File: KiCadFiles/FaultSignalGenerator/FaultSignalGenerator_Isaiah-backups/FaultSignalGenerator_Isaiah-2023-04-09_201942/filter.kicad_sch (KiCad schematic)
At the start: 65 parts

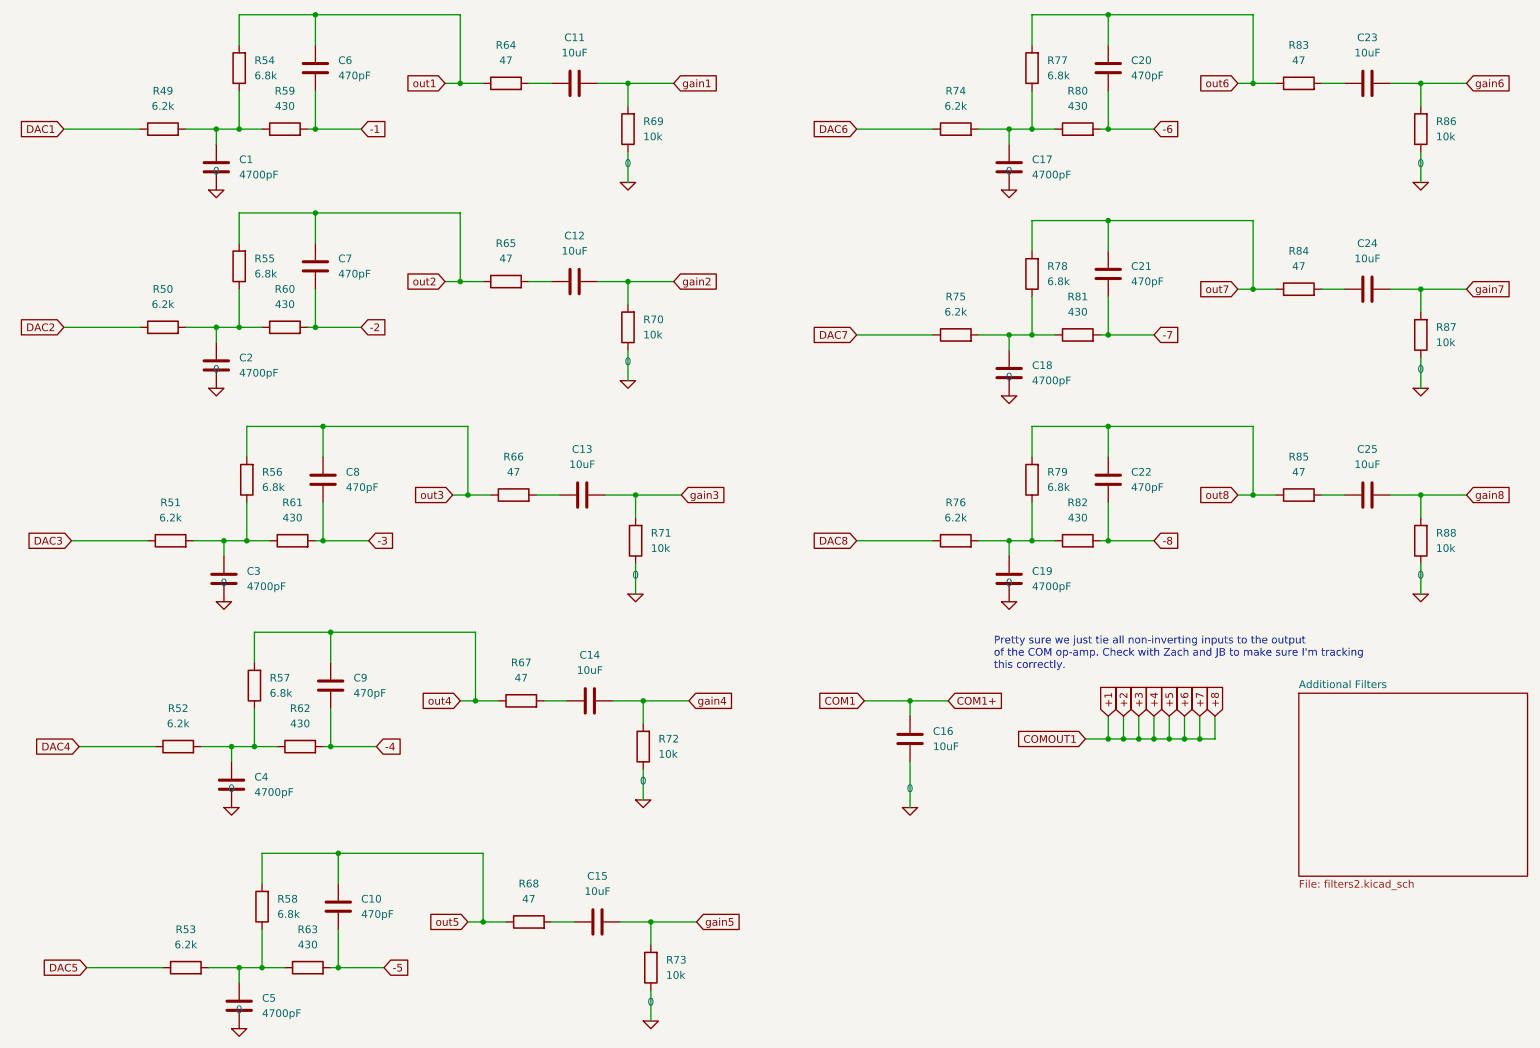
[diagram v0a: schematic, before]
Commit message: Finish schematic, start on PCB
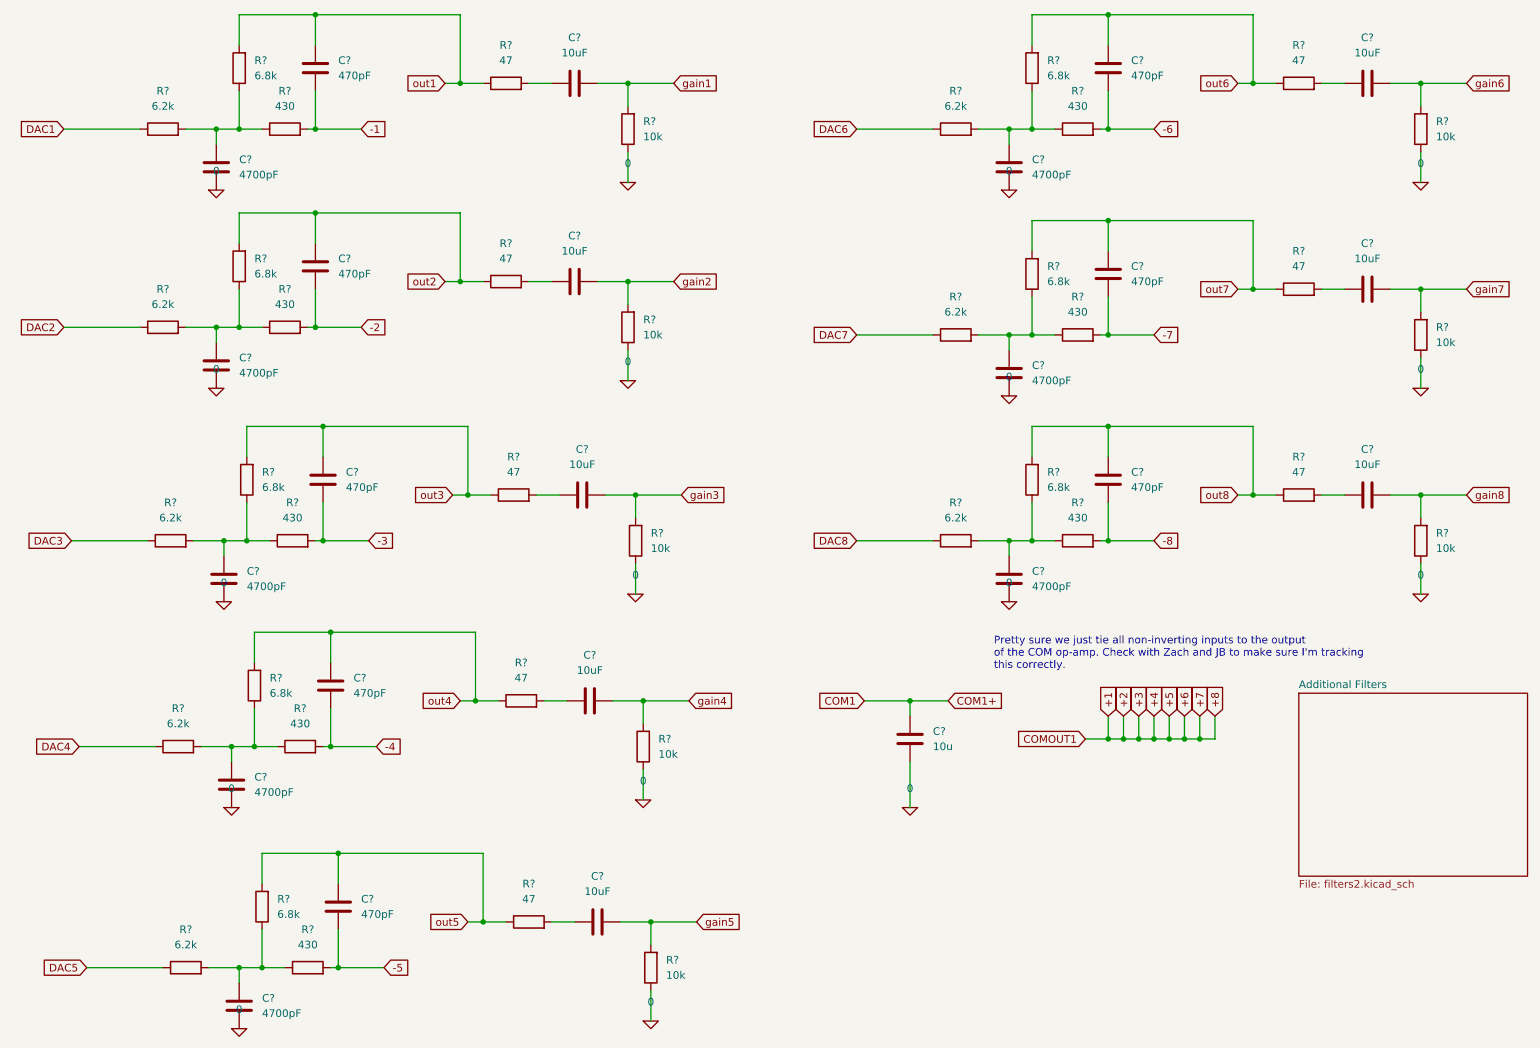
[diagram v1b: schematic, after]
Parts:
- C?: renamed from C16; value 10uF -> 10u; footprint Capacitor_SMD:C_1206_3216Metric_Pad1.33x1.80mm_HandSolder -> Capacitor_SMD:C_1812_4532Metric_Pad1.57x3.40mm_HandSolder; Spice_Model (none) -> 10u; Spice_Netlist_Enabled (none) -> Y; Spice_Primitive (none) -> C
- C?: renamed from C6; footprint Capacitor_SMD:C_1206_3216Metric_Pad1.33x1.80mm_HandSolder -> Capacitor_SMD:C_1812_4532Metric_Pad1.57x3.40mm_HandSolder; Spice_Model (none) -> 470p; Spice_Netlist_Enabled (none) -> Y; Spice_Primitive (none) -> C
- C?: renamed from C10; footprint Capacitor_SMD:C_1206_3216Metric_Pad1.33x1.80mm_HandSolder -> Capacitor_SMD:C_1812_4532Metric_Pad1.57x3.40mm_HandSolder; Spice_Model (none) -> 470p; Spice_Netlist_Enabled (none) -> Y; Spice_Primitive (none) -> C
- C?: renamed from C15; footprint Capacitor_SMD:C_1206_3216Metric_Pad1.33x1.80mm_HandSolder -> Capacitor_SMD:C_1812_4532Metric_Pad1.57x3.40mm_HandSolder; Spice_Model (none) -> 10u; Spice_Netlist_Enabled (none) -> Y; Spice_Primitive (none) -> C
- C?: renamed from C3; footprint Capacitor_SMD:C_1206_3216Metric_Pad1.33x1.80mm_HandSolder -> Capacitor_SMD:C_1812_4532Metric_Pad1.57x3.40mm_HandSolder; Spice_Model (none) -> 4700p; Spice_Netlist_Enabled (none) -> Y; Spice_Primitive (none) -> C
- C?: renamed from C20; footprint Capacitor_SMD:C_1206_3216Metric_Pad1.33x1.80mm_HandSolder -> Capacitor_SMD:C_1812_4532Metric_Pad1.57x3.40mm_HandSolder; Spice_Model (none) -> 470p; Spice_Netlist_Enabled (none) -> Y; Spice_Primitive (none) -> C
- C?: renamed from C18; footprint Capacitor_SMD:C_1206_3216Metric_Pad1.33x1.80mm_HandSolder -> Capacitor_SMD:C_1812_4532Metric_Pad1.57x3.40mm_HandSolder; Spice_Model (none) -> 4700p; Spice_Netlist_Enabled (none) -> Y; Spice_Primitive (none) -> C
- C?: renamed from C21; footprint Capacitor_SMD:C_1206_3216Metric_Pad1.33x1.80mm_HandSolder -> Capacitor_SMD:C_1812_4532Metric_Pad1.57x3.40mm_HandSolder; Spice_Model (none) -> 470p; Spice_Netlist_Enabled (none) -> Y; Spice_Primitive (none) -> C
- C?: renamed from C1; footprint Capacitor_SMD:C_1206_3216Metric_Pad1.33x1.80mm_HandSolder -> Capacitor_SMD:C_1812_4532Metric_Pad1.57x3.40mm_HandSolder; Spice_Model (none) -> 4700p; Spice_Netlist_Enabled (none) -> Y; Spice_Primitive (none) -> C
- C?: renamed from C7; footprint Capacitor_SMD:C_1206_3216Metric_Pad1.33x1.80mm_HandSolder -> Capacitor_SMD:C_1812_4532Metric_Pad1.57x3.40mm_HandSolder; Spice_Model (none) -> 470p; Spice_Netlist_Enabled (none) -> Y; Spice_Primitive (none) -> C
- C?: renamed from C8; footprint Capacitor_SMD:C_1206_3216Metric_Pad1.33x1.80mm_HandSolder -> Capacitor_SMD:C_1812_4532Metric_Pad1.57x3.40mm_HandSolder; Spice_Model (none) -> 470p; Spice_Netlist_Enabled (none) -> Y; Spice_Primitive (none) -> C
- C?: renamed from C25; footprint Capacitor_SMD:C_1206_3216Metric_Pad1.33x1.80mm_HandSolder -> Capacitor_SMD:C_1812_4532Metric_Pad1.57x3.40mm_HandSolder; Spice_Model (none) -> 10u; Spice_Netlist_Enabled (none) -> Y; Spice_Primitive (none) -> C
- C?: renamed from C9; footprint Capacitor_SMD:C_1206_3216Metric_Pad1.33x1.80mm_HandSolder -> Capacitor_SMD:C_1812_4532Metric_Pad1.57x3.40mm_HandSolder; Spice_Model (none) -> 470p; Spice_Netlist_Enabled (none) -> Y; Spice_Primitive (none) -> C
- C?: renamed from C12; footprint Capacitor_SMD:C_1206_3216Metric_Pad1.33x1.80mm_HandSolder -> Capacitor_SMD:C_1812_4532Metric_Pad1.57x3.40mm_HandSolder; Spice_Model (none) -> 10u; Spice_Netlist_Enabled (none) -> Y; Spice_Primitive (none) -> C
- C?: renamed from C14; footprint Capacitor_SMD:C_1206_3216Metric_Pad1.33x1.80mm_HandSolder -> Capacitor_SMD:C_1812_4532Metric_Pad1.57x3.40mm_HandSolder; Spice_Model (none) -> 10u; Spice_Netlist_Enabled (none) -> Y; Spice_Primitive (none) -> C
- C?: renamed from C5; footprint Capacitor_SMD:C_1206_3216Metric_Pad1.33x1.80mm_HandSolder -> Capacitor_SMD:C_1812_4532Metric_Pad1.57x3.40mm_HandSolder; Spice_Model (none) -> 4700p; Spice_Netlist_Enabled (none) -> Y; Spice_Primitive (none) -> C
- C?: renamed from C19; footprint Capacitor_SMD:C_1206_3216Metric_Pad1.33x1.80mm_HandSolder -> Capacitor_SMD:C_1812_4532Metric_Pad1.57x3.40mm_HandSolder; Spice_Model (none) -> 4700p; Spice_Netlist_Enabled (none) -> Y; Spice_Primitive (none) -> C
- C?: renamed from C13; footprint Capacitor_SMD:C_1206_3216Metric_Pad1.33x1.80mm_HandSolder -> Capacitor_SMD:C_1812_4532Metric_Pad1.57x3.40mm_HandSolder; Spice_Model (none) -> 10u; Spice_Netlist_Enabled (none) -> Y; Spice_Primitive (none) -> C
- C?: renamed from C17; footprint Capacitor_SMD:C_1206_3216Metric_Pad1.33x1.80mm_HandSolder -> Capacitor_SMD:C_1812_4532Metric_Pad1.57x3.40mm_HandSolder; Spice_Model (none) -> 4700p; Spice_Netlist_Enabled (none) -> Y; Spice_Primitive (none) -> C
- C?: renamed from C2; footprint Capacitor_SMD:C_1206_3216Metric_Pad1.33x1.80mm_HandSolder -> Capacitor_SMD:C_1812_4532Metric_Pad1.57x3.40mm_HandSolder; Spice_Model (none) -> 4700p; Spice_Netlist_Enabled (none) -> Y; Spice_Primitive (none) -> C
- C?: renamed from C22; footprint Capacitor_SMD:C_1206_3216Metric_Pad1.33x1.80mm_HandSolder -> Capacitor_SMD:C_1812_4532Metric_Pad1.57x3.40mm_HandSolder; Spice_Model (none) -> 470p; Spice_Netlist_Enabled (none) -> Y; Spice_Primitive (none) -> C
- C?: renamed from C24; footprint Capacitor_SMD:C_1206_3216Metric_Pad1.33x1.80mm_HandSolder -> Capacitor_SMD:C_1812_4532Metric_Pad1.57x3.40mm_HandSolder; Spice_Model (none) -> 10u; Spice_Netlist_Enabled (none) -> Y; Spice_Primitive (none) -> C
- C?: renamed from C23; footprint Capacitor_SMD:C_1206_3216Metric_Pad1.33x1.80mm_HandSolder -> Capacitor_SMD:C_1812_4532Metric_Pad1.57x3.40mm_HandSolder; Spice_Model (none) -> 10u; Spice_Netlist_Enabled (none) -> Y; Spice_Primitive (none) -> C
- C?: renamed from C11; footprint Capacitor_SMD:C_1206_3216Metric_Pad1.33x1.80mm_HandSolder -> Capacitor_SMD:C_1812_4532Metric_Pad1.57x3.40mm_HandSolder; Spice_Model (none) -> 10u; Spice_Netlist_Enabled (none) -> Y; Spice_Primitive (none) -> C
- C?: renamed from C4; footprint Capacitor_SMD:C_1206_3216Metric_Pad1.33x1.80mm_HandSolder -> Capacitor_SMD:C_1812_4532Metric_Pad1.57x3.40mm_HandSolder; Spice_Model (none) -> 4700p; Spice_Netlist_Enabled (none) -> Y; Spice_Primitive (none) -> C
- R?: renamed from R67; footprint Resistor_SMD:R_1206_3216Metric -> Resistor_SMD:R_0603_1608Metric_Pad0.98x0.95mm_HandSolder; Spice_Model (none) -> 47; Spice_Netlist_Enabled (none) -> Y; Spice_Primitive (none) -> R
- R?: renamed from R71; footprint Resistor_SMD:R_1206_3216Metric -> Resistor_SMD:R_0603_1608Metric_Pad0.98x0.95mm_HandSolder
- R?: renamed from R79; footprint Resistor_SMD:R_1206_3216Metric -> Resistor_SMD:R_0603_1608Metric_Pad0.98x0.95mm_HandSolder; Spice_Model (none) -> 6.8k; Spice_Netlist_Enabled (none) -> Y; Spice_Primitive (none) -> R
- R?: renamed from R50; footprint Resistor_SMD:R_1206_3216Metric -> Resistor_SMD:R_0603_1608Metric_Pad0.98x0.95mm_HandSolder; Spice_Model (none) -> 6.2k; Spice_Netlist_Enabled (none) -> Y; Spice_Primitive (none) -> R
- R?: renamed from R70; footprint Resistor_SMD:R_1206_3216Metric -> Resistor_SMD:R_0603_1608Metric_Pad0.98x0.95mm_HandSolder
- R?: renamed from R59; footprint Resistor_SMD:R_1206_3216Metric -> Resistor_SMD:R_0603_1608Metric_Pad0.98x0.95mm_HandSolder; Spice_Model (none) -> 430; Spice_Netlist_Enabled (none) -> Y; Spice_Primitive (none) -> R
- R?: renamed from R61; footprint Resistor_SMD:R_1206_3216Metric -> Resistor_SMD:R_0603_1608Metric_Pad0.98x0.95mm_HandSolder; Spice_Model (none) -> 430; Spice_Netlist_Enabled (none) -> Y; Spice_Primitive (none) -> R
- R?: renamed from R82; footprint Resistor_SMD:R_1206_3216Metric -> Resistor_SMD:R_0603_1608Metric_Pad0.98x0.95mm_HandSolder; Spice_Model (none) -> 430; Spice_Netlist_Enabled (none) -> Y; Spice_Primitive (none) -> R
- R?: renamed from R83; footprint Resistor_SMD:R_1206_3216Metric -> Resistor_SMD:R_0603_1608Metric_Pad0.98x0.95mm_HandSolder; Spice_Model (none) -> 47; Spice_Netlist_Enabled (none) -> Y; Spice_Primitive (none) -> R
- R?: renamed from R62; footprint Resistor_SMD:R_1206_3216Metric -> Resistor_SMD:R_0603_1608Metric_Pad0.98x0.95mm_HandSolder; Spice_Model (none) -> 430; Spice_Netlist_Enabled (none) -> Y; Spice_Primitive (none) -> R
- R?: renamed from R60; footprint Resistor_SMD:R_1206_3216Metric -> Resistor_SMD:R_0603_1608Metric_Pad0.98x0.95mm_HandSolder; Spice_Model (none) -> 430; Spice_Netlist_Enabled (none) -> Y; Spice_Primitive (none) -> R
- R?: renamed from R69; footprint Resistor_SMD:R_1206_3216Metric -> Resistor_SMD:R_0603_1608Metric_Pad0.98x0.95mm_HandSolder
- R?: renamed from R56; footprint Resistor_SMD:R_1206_3216Metric -> Resistor_SMD:R_0603_1608Metric_Pad0.98x0.95mm_HandSolder; Spice_Model (none) -> 6.8k; Spice_Netlist_Enabled (none) -> Y; Spice_Primitive (none) -> R
- R?: renamed from R68; footprint Resistor_SMD:R_1206_3216Metric -> Resistor_SMD:R_0603_1608Metric_Pad0.98x0.95mm_HandSolder; Spice_Model (none) -> 47; Spice_Netlist_Enabled (none) -> Y; Spice_Primitive (none) -> R
- R?: renamed from R58; footprint Resistor_SMD:R_1206_3216Metric -> Resistor_SMD:R_0603_1608Metric_Pad0.98x0.95mm_HandSolder; Spice_Model (none) -> 6.8k; Spice_Netlist_Enabled (none) -> Y; Spice_Primitive (none) -> R
- R?: renamed from R55; footprint Resistor_SMD:R_1206_3216Metric -> Resistor_SMD:R_0603_1608Metric_Pad0.98x0.95mm_HandSolder; Spice_Model (none) -> 6.8k; Spice_Netlist_Enabled (none) -> Y; Spice_Primitive (none) -> R
- R?: renamed from R85; footprint Resistor_SMD:R_1206_3216Metric -> Resistor_SMD:R_0603_1608Metric_Pad0.98x0.95mm_HandSolder; Spice_Model (none) -> 47; Spice_Netlist_Enabled (none) -> Y; Spice_Primitive (none) -> R
- R?: renamed from R66; footprint Resistor_SMD:R_1206_3216Metric -> Resistor_SMD:R_0603_1608Metric_Pad0.98x0.95mm_HandSolder; Spice_Model (none) -> 47; Spice_Netlist_Enabled (none) -> Y; Spice_Primitive (none) -> R
- R?: renamed from R72; footprint Resistor_SMD:R_1206_3216Metric -> Resistor_SMD:R_0603_1608Metric_Pad0.98x0.95mm_HandSolder
- R?: renamed from R88; footprint Resistor_SMD:R_1206_3216Metric -> Resistor_SMD:R_0603_1608Metric_Pad0.98x0.95mm_HandSolder
- R?: renamed from R49; footprint Resistor_SMD:R_1206_3216Metric -> Resistor_SMD:R_0603_1608Metric_Pad0.98x0.95mm_HandSolder; Spice_Model (none) -> 6.2k; Spice_Netlist_Enabled (none) -> Y; Spice_Primitive (none) -> R
- R?: renamed from R77; footprint Resistor_SMD:R_1206_3216Metric -> Resistor_SMD:R_0603_1608Metric_Pad0.98x0.95mm_HandSolder; Spice_Model (none) -> 6.8k; Spice_Netlist_Enabled (none) -> Y; Spice_Primitive (none) -> R
- R?: renamed from R76; footprint Resistor_SMD:R_1206_3216Metric -> Resistor_SMD:R_0603_1608Metric_Pad0.98x0.95mm_HandSolder; Spice_Model (none) -> 6.2k; Spice_Netlist_Enabled (none) -> Y; Spice_Primitive (none) -> R
- R?: renamed from R53; footprint Resistor_SMD:R_1206_3216Metric -> Resistor_SMD:R_0603_1608Metric_Pad0.98x0.95mm_HandSolder; Spice_Model (none) -> 6.2k; Spice_Netlist_Enabled (none) -> Y; Spice_Primitive (none) -> R
- R?: renamed from R64; footprint Resistor_SMD:R_1206_3216Metric -> Resistor_SMD:R_0603_1608Metric_Pad0.98x0.95mm_HandSolder; Spice_Model (none) -> 47; Spice_Netlist_Enabled (none) -> Y; Spice_Primitive (none) -> R
- R?: renamed from R81; footprint Resistor_SMD:R_1206_3216Metric -> Resistor_SMD:R_0603_1608Metric_Pad0.98x0.95mm_HandSolder; Spice_Model (none) -> 430; Spice_Netlist_Enabled (none) -> Y; Spice_Primitive (none) -> R
- R?: renamed from R51; footprint Resistor_SMD:R_1206_3216Metric -> Resistor_SMD:R_0603_1608Metric_Pad0.98x0.95mm_HandSolder; Spice_Model (none) -> 6.2k; Spice_Netlist_Enabled (none) -> Y; Spice_Primitive (none) -> R
- R?: renamed from R84; footprint Resistor_SMD:R_1206_3216Metric -> Resistor_SMD:R_0603_1608Metric_Pad0.98x0.95mm_HandSolder; Spice_Model (none) -> 47; Spice_Netlist_Enabled (none) -> Y; Spice_Primitive (none) -> R
- R?: renamed from R63; footprint Resistor_SMD:R_1206_3216Metric -> Resistor_SMD:R_0603_1608Metric_Pad0.98x0.95mm_HandSolder; Spice_Model (none) -> 430; Spice_Netlist_Enabled (none) -> Y; Spice_Primitive (none) -> R
- R?: renamed from R57; footprint Resistor_SMD:R_1206_3216Metric -> Resistor_SMD:R_0603_1608Metric_Pad0.98x0.95mm_HandSolder; Spice_Model (none) -> 6.8k; Spice_Netlist_Enabled (none) -> Y; Spice_Primitive (none) -> R
- R?: renamed from R80; footprint Resistor_SMD:R_1206_3216Metric -> Resistor_SMD:R_0603_1608Metric_Pad0.98x0.95mm_HandSolder; Spice_Model (none) -> 430; Spice_Netlist_Enabled (none) -> Y; Spice_Primitive (none) -> R
- R?: renamed from R86; footprint Resistor_SMD:R_1206_3216Metric -> Resistor_SMD:R_0603_1608Metric_Pad0.98x0.95mm_HandSolder
- R?: renamed from R52; footprint Resistor_SMD:R_1206_3216Metric -> Resistor_SMD:R_0603_1608Metric_Pad0.98x0.95mm_HandSolder; Spice_Model (none) -> 6.2k; Spice_Netlist_Enabled (none) -> Y; Spice_Primitive (none) -> R
- R?: renamed from R75; footprint Resistor_SMD:R_1206_3216Metric -> Resistor_SMD:R_0603_1608Metric_Pad0.98x0.95mm_HandSolder; Spice_Model (none) -> 6.2k; Spice_Netlist_Enabled (none) -> Y; Spice_Primitive (none) -> R
- R?: renamed from R87; footprint Resistor_SMD:R_1206_3216Metric -> Resistor_SMD:R_0603_1608Metric_Pad0.98x0.95mm_HandSolder
- R?: renamed from R78; footprint Resistor_SMD:R_1206_3216Metric -> Resistor_SMD:R_0603_1608Metric_Pad0.98x0.95mm_HandSolder; Spice_Model (none) -> 6.8k; Spice_Netlist_Enabled (none) -> Y; Spice_Primitive (none) -> R
- R?: renamed from R54; footprint Resistor_SMD:R_1206_3216Metric -> Resistor_SMD:R_0603_1608Metric_Pad0.98x0.95mm_HandSolder; Spice_Model (none) -> 6.8k; Spice_Netlist_Enabled (none) -> Y; Spice_Primitive (none) -> R
- R?: renamed from R73; footprint Resistor_SMD:R_1206_3216Metric -> Resistor_SMD:R_0603_1608Metric_Pad0.98x0.95mm_HandSolder
- R?: renamed from R74; footprint Resistor_SMD:R_1206_3216Metric -> Resistor_SMD:R_0603_1608Metric_Pad0.98x0.95mm_HandSolder; Spice_Model (none) -> 6.2k; Spice_Netlist_Enabled (none) -> Y; Spice_Primitive (none) -> R
- R?: renamed from R65; footprint Resistor_SMD:R_1206_3216Metric -> Resistor_SMD:R_0603_1608Metric_Pad0.98x0.95mm_HandSolder; Spice_Model (none) -> 47; Spice_Netlist_Enabled (none) -> Y; Spice_Primitive (none) -> R
